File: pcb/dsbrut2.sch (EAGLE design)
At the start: 14 parts, among them IC1 4175D, IC2 74HC125D, IC3 MEGA8-AI

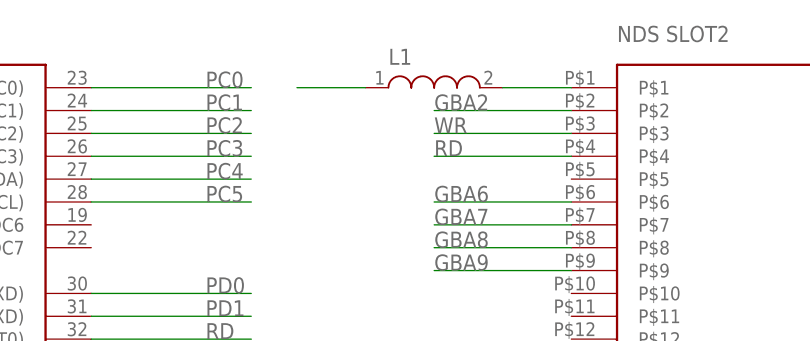
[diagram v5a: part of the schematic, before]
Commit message: Changed fuse label, moved a via, minor trace beautification
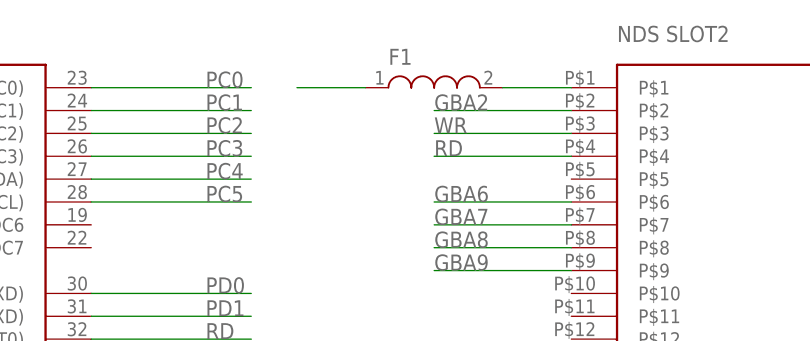
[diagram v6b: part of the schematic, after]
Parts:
- F1: value INDUCTOR-L1812 -> F1
- renumbered L1 to F1
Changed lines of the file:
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@@
 <part name="R1" library="rcl" deviceset="R-EU_" device="M0805"/>
 <part name="VSS1" library="supply1" deviceset="VSS" device=""/>
-<part name="L1" library="dp_devices" deviceset="INDUCTOR" device="-L1812"/>
+<part name="F1" library="dp_devices" deviceset="INDUCTOR" device="-L1812" value="F1"/>
 </parts>
 <sheets>
@@
 <instance part="R1" gate="G$1" x="170.18" y="86.36"/>
 <instance part="VSS1" gate="G$1" x="226.06" y="35.56" rot="R90"/>
-<instance part="L1" gate="L" x="195.58" y="149.86" smashed="yes">
+<instance part="F1" gate="L" x="195.58" y="149.86" smashed="yes">
 <attribute name="NAME" x="190.5" y="152.4" size="1.778" layer="95"/>
 </instance>
@@
 </segment>
 <segment>
-<pinref part="L1" gate="L" pin="1"/>
+<pinref part="F1" gate="L" pin="1"/>
 <wire x1="187.96" y1="149.86" x2="180.34" y2="149.86" width="0.1524" layer="91"/>
 </segment>
@@
 <segment>
 <pinref part="U$1" gate="G$1" pin="P$1"/>
-<pinref part="L1" gate="L" pin="2"/>
+<pinref part="F1" gate="L" pin="2"/>
 <wire x1="210.82" y1="149.86" x2="203.2" y2="149.86" width="0.1524" layer="91"/>
 </segment>

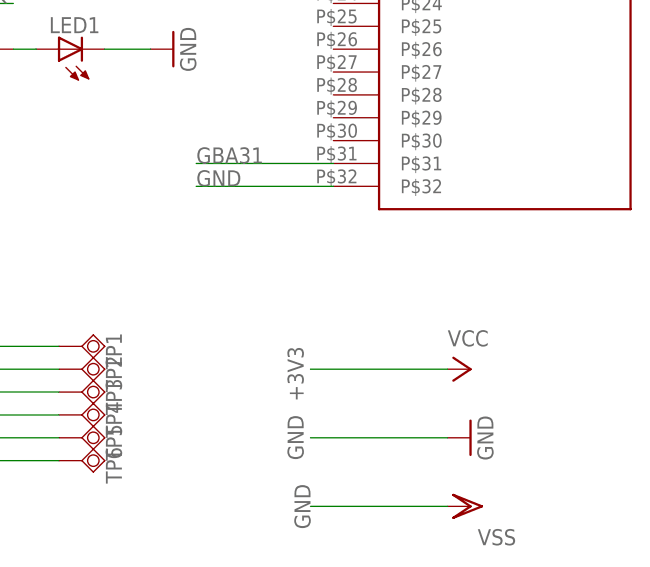
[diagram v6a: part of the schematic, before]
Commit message: power supply pin 16 on ic1
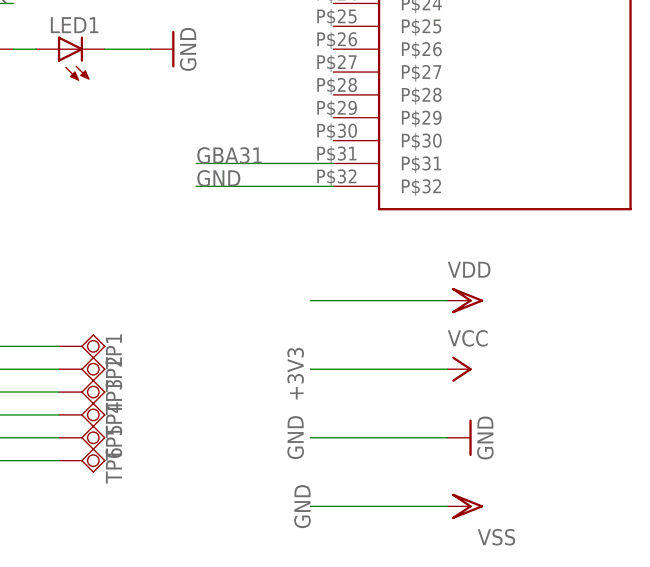
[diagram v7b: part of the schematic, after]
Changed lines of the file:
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@@
 <part name="VSS1" library="supply1" deviceset="VSS" device=""/>
 <part name="F1" library="dp_devices" deviceset="INDUCTOR" device="-L1812" value="F1"/>
+<part name="VDD1" library="supply1" deviceset="VDD" device=""/>
 </parts>
 <sheets>
@@
 <attribute name="NAME" x="190.5" y="152.4" size="1.778" layer="95"/>
 </instance>
+<instance part="VDD1" gate="G$1" x="226.06" y="58.42" rot="R270"/>
 </instances>
 <busses>
@@
 <wire x1="187.96" y1="149.86" x2="180.34" y2="149.86" width="0.1524" layer="91"/>
 </segment>
+<segment>
+<pinref part="VDD1" gate="G$1" pin="VDD"/>
+<wire x1="223.52" y1="58.42" x2="208.28" y2="58.42" width="0.1524" layer="91"/>
+</segment>
 </net>

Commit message: Made pin1 of the ICSP connector square
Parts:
- TP3: value TPSQTP16R -> TPSQTP16SQ; device testpad:TPSQTP16R -> testpad:TPSQTP16SQ
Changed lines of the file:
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@@
 <grid distance="0.1" unitdist="inch" unit="inch" style="lines" multiple="1" display="no" altdistance="0.01" altunitdist="inch" altunit="inch"/>
 <layers>
-<layer number="1" name="Top" color="4" fill="1" visible="no" active="no"/>
-<layer number="16" name="Bottom" color="1" fill="1" visible="no" active="no"/>
-<layer number="17" name="Pads" color="2" fill="1" visible="no" active="no"/>
-<layer number="18" name="Vias" color="2" fill="1" visible="no" active="no"/>
-<layer number="19" name="Unrouted" color="6" fill="1" visible="no" active="no"/>
-<layer number="20" name="Dimension" color="15" fill="1" visible="no" active="no"/>
-<layer number="21" name="tPlace" color="7" fill="1" visible="no" active="no"/>
-<layer number="22" name="bPlace" color="7" fill="1" visible="no" active="no"/>
-<layer number="23" name="tOrigins" color="15" fill="1" visible="no" active="no"/>
-<layer number="24" name="bOrigins" color="15" fill="1" visible="no" active="no"/>
-<layer number="25" name="tNames" color="7" fill="1" visible="no" active="no"/>
-<layer number="26" name="bNames" color="7" fill="1" visible="no" active="no"/>
-<layer number="27" name="tValues" color="7" fill="1" visible="no" active="no"/>
-<layer number="28" name="bValues" color="7" fill="1" visible="no" active="no"/>
+<layer number="1" name="Top" color="4" fill="1" visible="yes" active="no"/>
+<layer number="16" name="Bottom" color="1" fill="1" visible="yes" active="no"/>
+<layer number="17" name="Pads" color="2" fill="1" visible="yes" active="no"/>
+<layer number="18" name="Vias" color="2" fill="1" visible="yes" active="no"/>
+<layer number="19" name="Unrouted" color="6" fill="1" visible="yes" active="no"/>
+<layer number="20" name="Dimension" color="15" fill="1" visible="yes" active="no"/>
+<layer number="21" name="tPlace" color="7" fill="1" visible="yes" active="no"/>
+<layer number="22" name="bPlace" color="7" fill="1" visible="yes" active="no"/>
+<layer number="23" name="tOrigins" color="15" fill="1" visible="yes" active="no"/>
+<layer number="24" name="bOrigins" color="15" fill="1" visible="yes" active="no"/>
+<layer number="25" name="tNames" color="7" fill="1" visible="yes" active="no"/>
+<layer number="26" name="bNames" color="7" fill="1" visible="yes" active="no"/>
+<layer number="27" name="tValues" color="7" fill="1" visible="yes" active="no"/>
+<layer number="28" name="bValues" color="7" fill="1" visible="yes" active="no"/>
 <layer number="29" name="tStop" color="7" fill="3" visible="no" active="no"/>
 <layer number="30" name="bStop" color="7" fill="6" visible="no" active="no"/>
@@
 <layer number="35" name="tGlue" color="7" fill="4" visible="no" active="no"/>
 <layer number="36" name="bGlue" color="7" fill="5" visible="no" active="no"/>
-<layer number="37" name="tTest" color="7" fill="1" visible="no" active="no"/>
-<layer number="38" name="bTest" color="7" fill="1" visible="no" active="no"/>
+<layer number="37" name="tTest" color="7" fill="1" visible="yes" active="no"/>
+<layer number="38" name="bTest" color="7" fill="1" visible="yes" active="no"/>
 <layer number="39" name="tKeepout" color="4" fill="11" visible="no" active="no"/>
 <layer number="40" name="bKeepout" color="1" fill="11" visible="no" active="no"/>
@@
 <layer number="44" name="Drills" color="7" fill="1" visible="no" active="no"/>
 <layer number="45" name="Holes" color="7" fill="1" visible="no" active="no"/>
-<layer number="46" name="Milling" color="3" fill="1" visible="no" active="no"/>
-<layer number="47" name="Measures" color="7" fill="1" visible="no" active="no"/>
-<layer number="48" name="Document" color="7" fill="1" visible="no" active="no"/>
-<layer number="49" name="Reference" color="7" fill="1" visible="no" active="no"/>
-<layer number="50" name="dxf" color="7" fill="1" visible="no" active="no"/>
-<layer number="51" name="tDocu" color="7" fill="1" visible="no" active="no"/>
-<layer number="52" name="bDocu" color="7" fill="1" visible="no" active="no"/>
-<layer number="53" name="tGND_GNDA" color="7" fill="9" visible="no" active="no"/>
-<layer number="54" name="bGND_GNDA" color="1" fill="9" visible="no" active="no"/>
-<layer number="56" name="wert" color="7" fill="1" visible="no" active="no"/>
+<layer number="46" name="Milling" color="3" fill="1" visible="yes" active="no"/>
+<layer number="47" name="Measures" color="7" fill="1" visible="yes" active="no"/>
+<layer number="48" name="Document" color="7" fill="1" visible="yes" active="no"/>
+<layer number="49" name="Reference" color="7" fill="1" visible="yes" active="no"/>
+<layer number="50" name="dxf" color="7" fill="1" visible="yes" active="no"/>
+<layer number="51" name="tDocu" color="7" fill="1" visible="yes" active="no"/>
+<layer number="52" name="bDocu" color="7" fill="1" visible="yes" active="no"/>
+<layer number="53" name="tGND_GNDA" color="7" fill="9" visible="yes" active="no"/>
+<layer number="54" name="bGND_GNDA" color="1" fill="9" visible="yes" active="no"/>
+<layer number="56" name="wert" color="7" fill="1" visible="yes" active="no"/>
 <layer number="91" name="Nets" color="2" fill="1" visible="yes" active="yes"/>
 <layer number="92" name="Busses" color="1" fill="1" visible="yes" active="yes"/>
@@
 <part name="TP1" library="testpad" deviceset="TPSQ" device="TP16R" value="TPSQTP16R"/>
 <part name="TP2" library="testpad" deviceset="TPSQ" device="TP16R" value="TPSQTP16R"/>
-<part name="TP3" library="testpad" deviceset="TPSQ" device="TP16R" value="TPSQTP16R"/>
+<part name="TP3" library="testpad" deviceset="TPSQ" device="TP16SQ" value="TPSQTP16SQ"/>
 <part name="TP4" library="testpad" deviceset="TPSQ" device="TP16R" value="TPSQTP16R"/>
 <part name="TP5" library="testpad" deviceset="TPSQ" device="TP16R" value="TPSQTP16R"/>
